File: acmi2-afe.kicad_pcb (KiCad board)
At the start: 6 copper layers, 241.3 x 76.2 mm, 131 parts, among them J1 6469028-1, J2 6469028-1, J3 6469028-1, J4 132134, J5 5499922-4, J6 39301022, J7 5499922-4, Q1 NX7002BKW, T1 T1-1T-KK81, U1 200MHz, U10 TPS3850H50DRCR, U2 LTC2107CUK-PBF, U3 TPS7A8500RGRT, U4 TPSM82866AA0HRDMR, U5 TPS7A8500RGRT, U6 TPS259540DSGR, U7 SN74LVC16T245DGGR, U8 CAT25320VI-GT3

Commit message: Add fab drawings
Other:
- board text added: "0"
- board text added: "0 mm"
- board text added: "0.01 mm"
- board text added: "0.02"
- board text added: "0.035 mm"
- board text added: "0.13 mm"
- board text added: "0.1524 mm / 0.1500 mm"
- board text added: "0.196 mm"
- board text added: "0.43 mm"
- board text added: "1"
- board text added: "1.5460 mm"
- board text added: "2116"
- board text added: "241.3000 mm x 76.2000 mm"
- board text added: "3.3"
- board text added: "4.45"
- board text added: "4.5"
- board text added: "4.6"
- board text added: "4.74"
- board text added: "6"
- board text added: "7628"
- board text added: "ACMI-2 AFE"
- board text added: "B.Cu - L6 Signal"
- board text added: "B.Mask"
- board text added: "B.Paste"
- board text added: "B.Silkscreen"
- board text added: "Bottom Silk Screen"
- board text added: "Bottom Solder Mask"
- board text added: "Bottom Solder Paste"
- board text added: "Color"
- board text added: "Controlled Impedance Top and Bottom Layers 1 Top Sig Edge coupled microstrip .17/.15 mm 100 Ohm differential 10% 2 In1 GND 3 In2 PWR 4 In3 Sig 5 In4 GND 6 Bot Sig Edge coupled microstrip .17/.15 mm 100 Ohm differential 10%"
- board text added: "DK"
- board text added: "Dielectric"
- board text added: "Epsilon R"
- board text added: "F.Cu - L1 Signal"
- board text added: "F.Mask"
- board text added: "F.Paste"
- board text added: "F.Silkscreen"
- board text added: "FR4 natural"
- board text added: "Green"
- board text added: "In1.Cu - L2 GND"
- board text added: "In2.Cu - L3 Pwr"
- board text added: "In3.Cu - L4 Signal"
- board text added: "In4.Cu - L5 GND"
- board text added: "Layer Name"
- board text added: "Loss Tangent"
- board text added: "Material"
- board text added: "Not specified"
- board text added: "Thickness (mm)"
- board text added: "Top Silk Screen"
- board text added: "Top Solder Mask"
- board text added: "Top Solder Paste"
- board text added: "Type"
- board text added: "copper"
- board text added: "core"
- board text added: "prepreg"
- board text removed: "0.0000 mm / 0.0000 mm"
- board text removed: "1.6000 mm"
- board text removed: "10"
- board text removed: "241.3000 mm x 255.0000 mm"
- board text removed: "zuPSC Carrier Board"

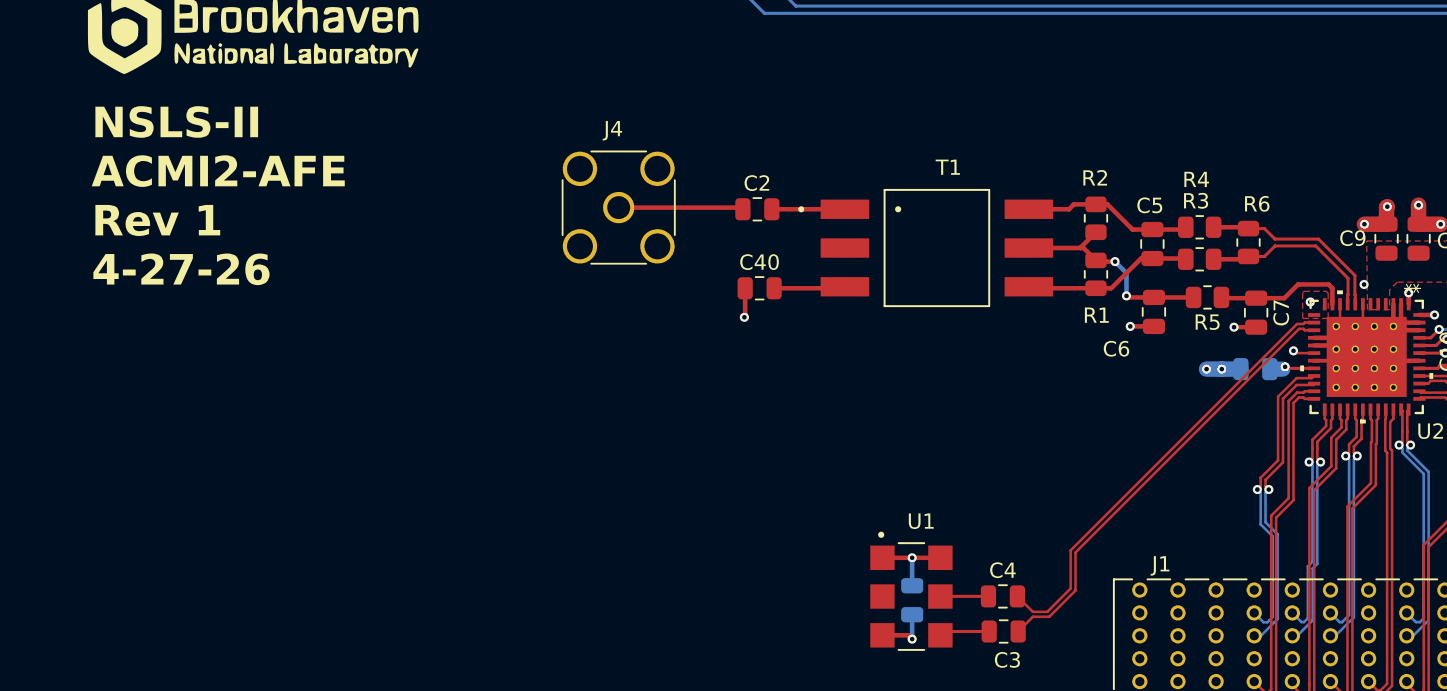
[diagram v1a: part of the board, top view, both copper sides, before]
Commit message: Add stitching vias, finalize gerbers
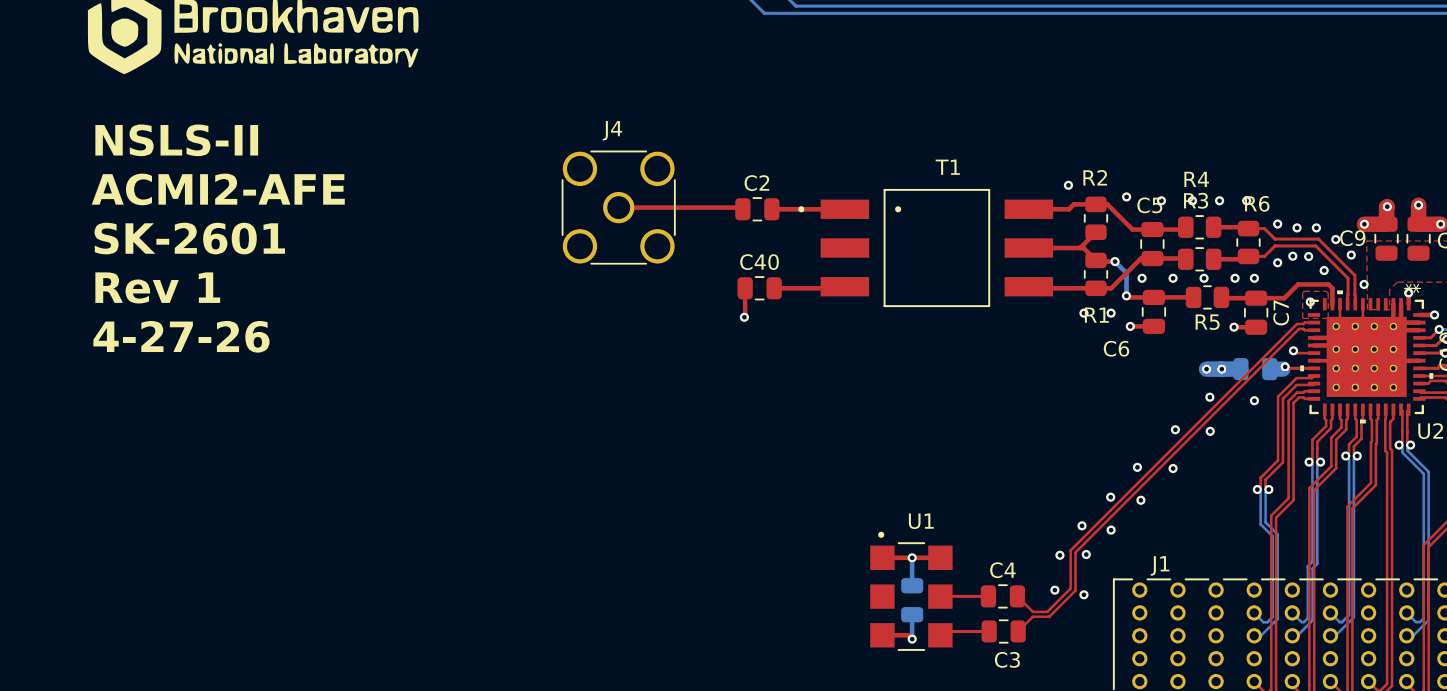
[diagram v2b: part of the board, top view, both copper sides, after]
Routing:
- net GND: vias 98 -> 134
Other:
- board text added: "NSLS-II ACMI2-AFE SK-2601 Rev 1 4-27-26"
- board text removed: "NSLS-II ACMI2-AFE Rev 1 4-27-26"

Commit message: Add drawing borders, moved copper pours inside board edge, add fab notes, update bnl logo
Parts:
- removed G***: LOGO, myparts:bnl_logo
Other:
- board text added: "*"
- board text added: "0 mils"
- board text added: "0.3937 mils"
- board text added: "1 oz COPPER"
- board text added: "1.37795 mils"
- board text added: "11.81 mils"
- board text added: "16.92913 mils"
- board text added: "5.11811 mils"
- board text added: "5.91 mil"
- board text added: "6 LAYER DETAIL ( DIELECTRIC CONSTANT = 4.3 )"
- board text added: "6 mil"
- board text added: "6.00 mils / 5.91 mils"
- board text added: "60.87 mils"
- board text added: "7.71654 mils"
- board text added: "9500.00 mils x 3000.00 mils"
- board text added: "ALL HOLES 0.610MM / 0.0240{dblquote} PRESS FIT TO −0.84 mil / +1.68 mil"
- board text added: "ASSEMBLY BOTTOM ${DRAWING_NUMBER-PREFIX}-${DRAWING-ASSY_SUFFIX} REV-${REVISION_NUM} ${DRAWN_BY_DATE}"
- board text added: "ASSEMBLY TOP ${DRAWING_NUMBER-PREFIX}-${DRAWING-ASSY_SUFFIX} REV-${REVISION_NUM} ${DRAWN_BY_DATE}"
- board text added: "C1"
- board text added: "C10"
- board text added: "C11"
- board text added: "C12"
- board text added: "C13"
- board text added: "C14"
- board text added: "C15"
- board text added: "C16"
- board text added: "C17"
- board text added: "C18"
- board text added: "C19"
- board text added: "C2"
- board text added: "C20"
- board text added: "C21"
- board text added: "C22"
- board text added: "C23"
- board text added: "C24"
- board text added: "C25"
- board text added: "C26"
- board text added: "C27"
- board text added: "C28"
- board text added: "C29"
- board text added: "C3"
- board text added: "C30"
- board text added: "C31"
- board text added: "C32"
- board text added: "C33"
- board text added: "C34"
- board text added: "C35"
- board text added: "C36"
- board text added: "C37"
- board text added: "C38"
- board text added: "C39"
- board text added: "C4"
- board text added: "C40"
- board text added: "C44"
- board text added: "C45"
- board text added: "C46"
- board text added: "C5"
- board text added: "C6"
- board text added: "C7"
- board text added: "C8"
- board text added: "C9"
- board text added: "CORE MATERIAL"
- board text added: "Controlled Impedance Top and Bottom Layers 1 Top Sig Edge coupled microstrip .17/.15 mm 100 Ohm differential 10% 2 In1 GND 3 In2 PWR 4 In3 Sig 5 In4 GND 6 Bot Sig Edge coupled microstrip .17/.15 mm 100 Ohm differential 10% THESE NUMBERS ARE FOR REFERENCE ONLY. FINAL WIDTHS AND SEPERATIONS TO ACHIEVE 100 OHMS DIFFERENTIAL IMPEDANCE SHALL BE THE RESPONSIBILITY OF THE BOARD FABRICATOR."
- board text added: "D1"
- board text added: "D10"
- board text added: "D11"
- board text added: "D12"
- board text added: "D13"
- board text added: "D14"
- board text added: "D15"
- board text added: "D16"
- board text added: "D17"
- board text added: "D2"
- board text added: "D3"
- board text added: "D4"
- board text added: "D5"
- board text added: "D6"
- board text added: "D7"
- board text added: "D8"
- board text added: "D9"
- board text added: "DRC'S MUST BE RUN ON THE GERBERS PRIOR TO BUILDING BOARDS 1.) BOARD MATERIAL: (SEE STACKUP BELOW) □ RF35 □ RO4003 □ FR-4 □ RO4350 □ 4000-13EP 2.) BOARD STACKUP □ COMPONENTS ON TOP SIDE ONLY □ COMPONENTS ON BOTH SIDES ____ LAYERS FINISHED OVERALL THICKNESS: □ .031 +/- .005 □ .062 +/- .005 □ .093 +/- .005 □ .125 +/- .005 3.) COPPER WEIGHT: EXTERNAL LAYERS: (SEE STACKUP BELOW) OUNCE FINISHED INTERNA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"
- board text added: "DRILL DRAWING ${DRAWING_NUMBER-PREFIX}-${DRAWING-FAB_SUFFIX} REV-${REVISION_NUM} ${DRAWN_BY_DATE}"
- board text added: "FABRICATION NOTES"
- board text added: "GND"
- board text added: "J1"
- board text added: "J2"
- board text added: "J3"
- board text added: "J4"
- board text added: "J5"
- board text added: "J6"
- board text added: "J7"
- board text added: "L1"
- board text added: "L2"
- board text added: "LAYER 1 COMPONENT SIDE ${DRAWING_NUMBER-PREFIX}-${DRAWING-ASSY_SUFFIX} REV-${REVISION_NUM} ${DRAWN_BY_DATE}"
- board text added: "LAYER 2 INTERNAL PLANE ${DRAWING_NUMBER-PREFIX}-${DRAWING-ASSY_SUFFIX} REV-${REVISION_NUM} ${DRAWN_BY_DATE}"
- board text added: "LAYER 3 INTERNAL PLANE ${DRAWING_NUMBER-PREFIX}-${DRAWING-ASSY_SUFFIX} REV-${REVISION_NUM} ${DRAWN_BY_DATE}"
- board text added: "LAYER 4 INTERNAL SIGNAL ${DRAWING_NUMBER-PREFIX}-${DRAWING-ASSY_SUFFIX} REV-${REVISION_NUM} ${DRAWN_BY_DATE}"
- board text added: "LAYER 5 INTERNAL PLANE ${DRAWING_NUMBER-PREFIX}-${DRAWING-ASSY_SUFFIX} REV-${REVISION_NUM} ${DRAWN_BY_DATE}"
- board text added: "LAYER 6 BOTTOM SIDE ${DRAWING_NUMBER-PREFIX}-${DRAWING-ASSY_SUFFIX} REV-${REVISION_NUM} ${DRAWN_BY_DATE}"
- board text added: "LY01"
- board text added: "LY02"
- board text added: "LY03"
- board text added: "LY04"
- board text added: "LY05"
- board text added: "LY06"
- board text added: "NOTES: UNLESS OTHERWISE SPECIFIED 1. FOR COMPONENT VALUES AND PART NUMBERS SEE PARTS LIST. 2. INSPECTION CRITERIA FOR ACCEPTANCE OF PRINTED CIRCUIT ASSEMBLY TO BE IAW IPC-A-610, CLASS 2 AND J-STD-001A, CLASS 2, UNLESS OTHERWISE NOTED ON THIS DRAWING. 3. MARK SERIAL NUMBER IN DESIGNATED AREA ACCORDING TO INSTRUCTIONS ON STATEMENT OF WORK (SOW)"
- board text added: "PASTE MASK BOTTOM ${DRAWING_NUMBER-PREFIX}-${DRAWING-ASSY_SUFFIX} REV-${REVISION_NUM} ${DRAWN_BY_DATE}"
- board text added: "PASTE MASK TOP ${DRAWING_NUMBER-PREFIX}-${DRAWING-ASSY_SUFFIX} REV-${REVISION_NUM} ${DRAWN_BY_DATE}"
- board text added: "PMB"
- board text added: "PMT"
- board text added: "PREPREG MATERIAL"
- board text added: "Q1"
- board text added: "R1"
- board text added: "R10"
- board text added: "R11"
- board text added: "R12"
- board text added: "R13"
- board text added: "R14"
- board text added: "R15"
- board text added: "R16"
- board text added: "R17"
- board text added: "R18"
- board text added: "R19"
- board text added: "R2"
- board text added: "R20"
- board text added: "R21"
- board text added: "R22"
- board text added: "R23"
- board text added: "R24"
- board text added: "R25"
- board text added: "R26"
- board text added: "R27"
- board text added: "R3"
- board text added: "R36"
- board text added: "R37"
- board text added: "R38"
- board text added: "R39"
- board text added: "R4"
- board text added: "R40"
- board text added: "R41"
- board text added: "R42"
- board text added: "R43"
- board text added: "R44"
- board text added: "R45"
- board text added: "R5"
- board text added: "R6"
- board text added: "R7"
- board text added: "R8"
- board text added: "R9"
- board text added: "SILKSCREEN (BOTTOM SIDE)"
- board text added: "SILKSCREEN (TOP SIDE)"
- board text added: "SILKSCREEN BOTTOM ${DRAWING_NUMBER-PREFIX}-${DRAWING-ASSY_SUFFIX} REV-${REVISION_NUM} ${DRAWN_BY_DATE}"
- board text added: "SILKSCREEN TOP ${DRAWING_NUMBER-PREFIX}-${DRAWING-ASSY_SUFFIX} REV-${REVISION_NUM} ${DRAWN_BY_DATE} (VIEWED THRU COMPONENT SIDE)"
- board text added: "SMB"
- board text added: "SMT"
- board text added: "SOLDER MASK (BOTTOM SIDE)"
- board text added: "SOLDER MASK (TOP SIDE)"
- board text added: "SOLDER MASK BOTTOM ${DRAWING_NUMBER-PREFIX}-${DRAWING-ASSY_SUFFIX} REV-${REVISION_NUM} ${DRAWN_BY_DATE}"
- board text added: "SOLDER MASK TOP ${DRAWING_NUMBER-PREFIX}-${DRAWING-ASSY_SUFFIX} REV-${REVISION_NUM} ${DRAWN_BY_DATE}"
- board text added: "SSB"
- board text added: "SST"
- board text added: "T1"
- board text added: "TP1"
- board text added: "TP2"
- board text added: "TP3"
- board text added: "TP4"
- board text added: "TP5"
- board text added: "Thickness (mils)"
- board text added: "U1"
- board text added: "U10"
- board text added: "U2"
- board text added: "U3"
- board text added: "U4"
- board text added: "U5"
- board text added: "U6"
- board text added: "U7"
- board text added: "U8"
- board text added: "Yes"
- board text added: "x"
- board text removed: "0 mm"
- board text removed: "0.01 mm"
- board text removed: "0.035 mm"
- board text removed: "0.13 mm"
- board text removed: "0.1524 mm / 0.1500 mm"
- board text removed: "0.196 mm"
- board text removed: "0.3000 mm"
- board text removed: "0.43 mm"
- board text removed: "1.5460 mm"
- board text removed: "241.3000 mm x 76.2000 mm"
- board text removed: "ACMI-2 AFE"
- board text removed: "B.Cu - L6 Signal"
- board text removed: "B.Mask"
- board text removed: "B.Paste"
- board text removed: "B.Silkscreen"
- board text removed: "Controlled Impedance Top and Bottom Layers 1 Top Sig Edge coupled microstrip .17/.15 mm 100 Ohm differential 10% 2 In1 GND 3 In2 PWR 4 In3 Sig 5 In4 GND 6 Bot Sig Edge coupled microstrip .17/.15 mm 100 Ohm differential 10%"
- board text removed: "F.Cu - L1 Signal"
- board text removed: "F.Mask"
- board text removed: "F.Paste"
- board text removed: "F.Silkscreen"
- board text removed: "In1.Cu - L2 GND"
- board text removed: "In2.Cu - L3 Pwr"
- board text removed: "In3.Cu - L4 Signal"
- board text removed: "In4.Cu - L5 GND"
- board text removed: "Thickness (mm)"
